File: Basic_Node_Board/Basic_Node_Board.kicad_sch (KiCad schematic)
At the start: 0 parts

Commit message: mh_initial_node_board_edits
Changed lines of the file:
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@@
 	(sheet
 		(at 31.75 88.9)
-		(size 72.39 45.72)
+		(size 90.17 76.2)
 		(fields_autoplaced yes)
 		(stroke
@@
 		)
 		(property "Sheetfile" "microcontroller.kicad_sch"
-			(at 31.75 135.2046 0)
+			(at 31.75 165.6846 0)
 			(effects
 				(font

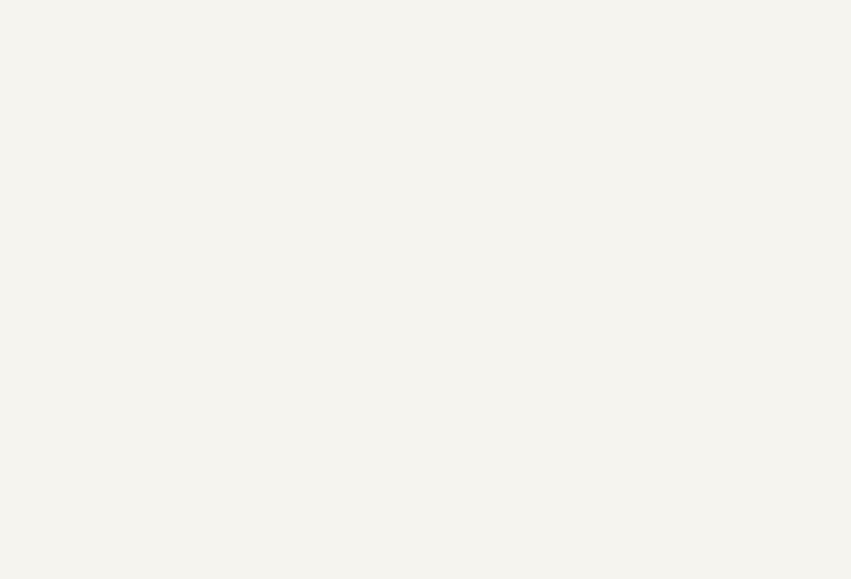
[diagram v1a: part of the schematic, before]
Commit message: Adding Buck Converter Schematic/Footprints
Added footprints to main pcb. Removing duplicate footprints (might cause problems, we will find out).
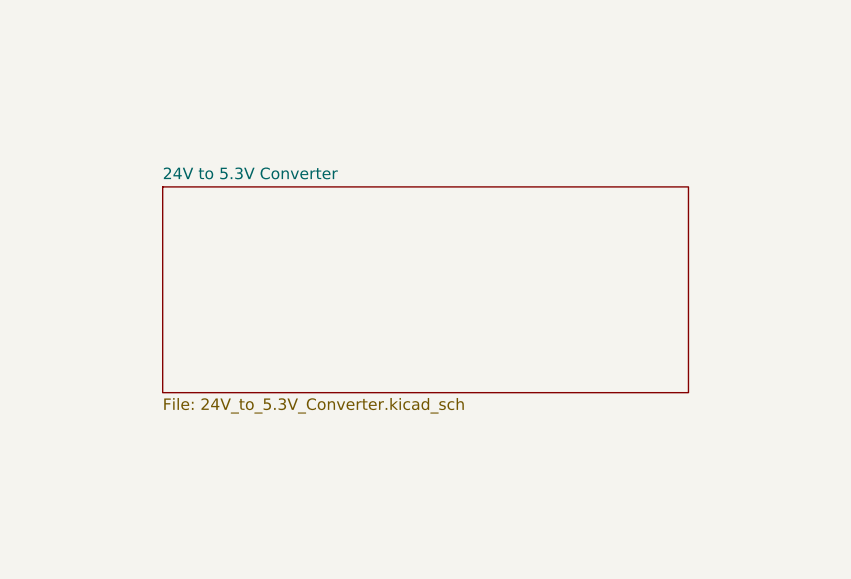
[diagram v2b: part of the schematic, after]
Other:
- added sheet 24V to 5.3V Converter (24V_to_5.3V_Converter.kicad_sch)
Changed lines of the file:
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@@
 (kicad_sch
-	(version 20231120)
+	(version 20250114)
 	(generator "eeschema")
-	(generator_version "8.0")
+	(generator_version "9.0")
 	(paper "A4")
 	(title_block
@@
 	)
 	(sheet
+		(at 156.21 95.25)
+		(size 58.42 22.86)
+		(exclude_from_sim no)
+		(in_bom yes)
+		(on_board yes)
+		(dnp no)
+		(fields_autoplaced yes)
+		(stroke
+			(width 0.1524)
+			(type solid)
+		)
+		(fill
+			(color 0 0 0 0.0000)
+		)
+		(property "Sheetname" "24V to 5.3V Converter"
+			(at 156.21 94.5384 0)
+			(effects
+				(font
+					(size 1.27 1.27)
+				)
+				(justify left bottom)
+			)
+		)
+		(property "Sheetfile" "24V_to_5.3V_Converter.kicad_sch"
+			(at 156.21 118.6946 0)
+			(effects
+				(font
+					(size 1.27 1.27)
+				)
+				(justify left top)
+			)
+		)
+		(instances
+			(project "Basic_Node_Board"
+				(path "/9602f2a9-59de-4c89-af09-0033871e87a5"
+					(page "5")
+				)
+			)
+		)
+	)
+	(sheet
 		(at 152.4 21.59)
 		(size 83.82 45.72)
+		(exclude_from_sim no)
+		(in_bom yes)
+		(on_board yes)
+		(dnp no)
 		(fields_autoplaced yes)
 		(stroke
@@
 		(at 31.75 88.9)
 		(size 90.17 76.2)
+		(exclude_from_sim no)
+		(in_bom yes)
+		(on_board yes)
+		(dnp no)
 		(fields_autoplaced yes)
 		(stroke
@@
 		(at 31.75 22.86)
 		(size 66.04 45.72)
+		(exclude_from_sim no)
+		(in_bom yes)
+		(on_board yes)
+		(dnp no)
 		(fields_autoplaced yes)
 		(stroke
@@
 		)
 	)
+	(embedded_fonts no)
 )

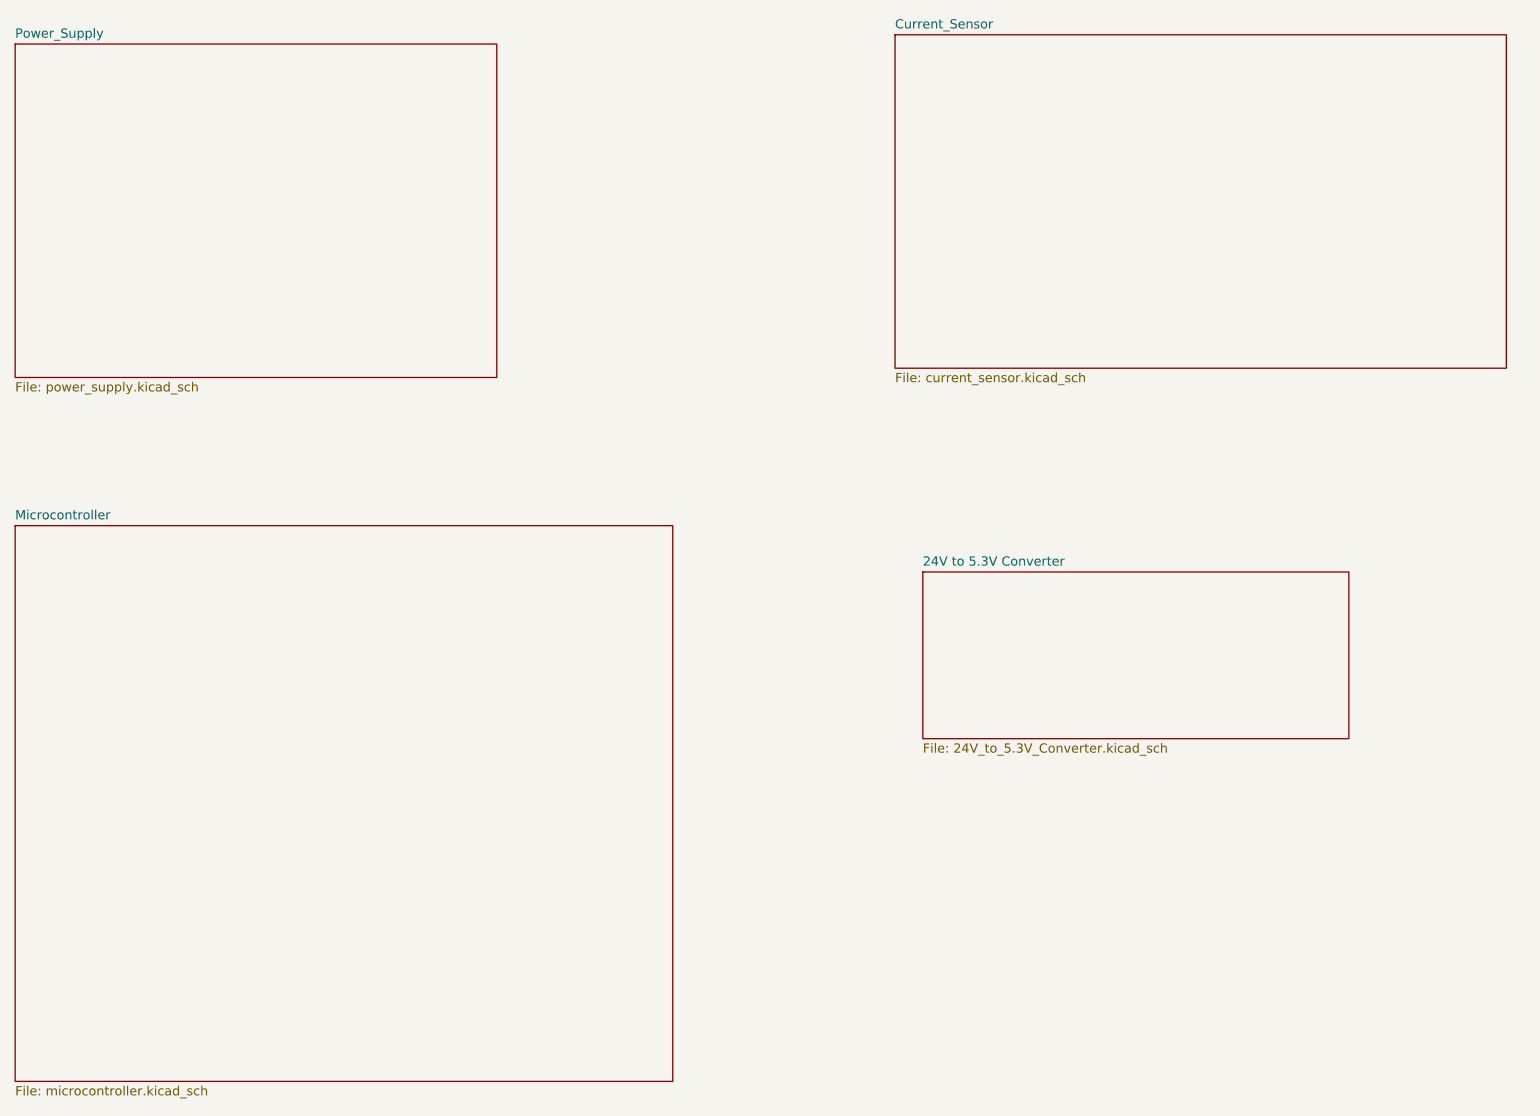
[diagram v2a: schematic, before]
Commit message: Power Distribution PCB KiCAD Schematic
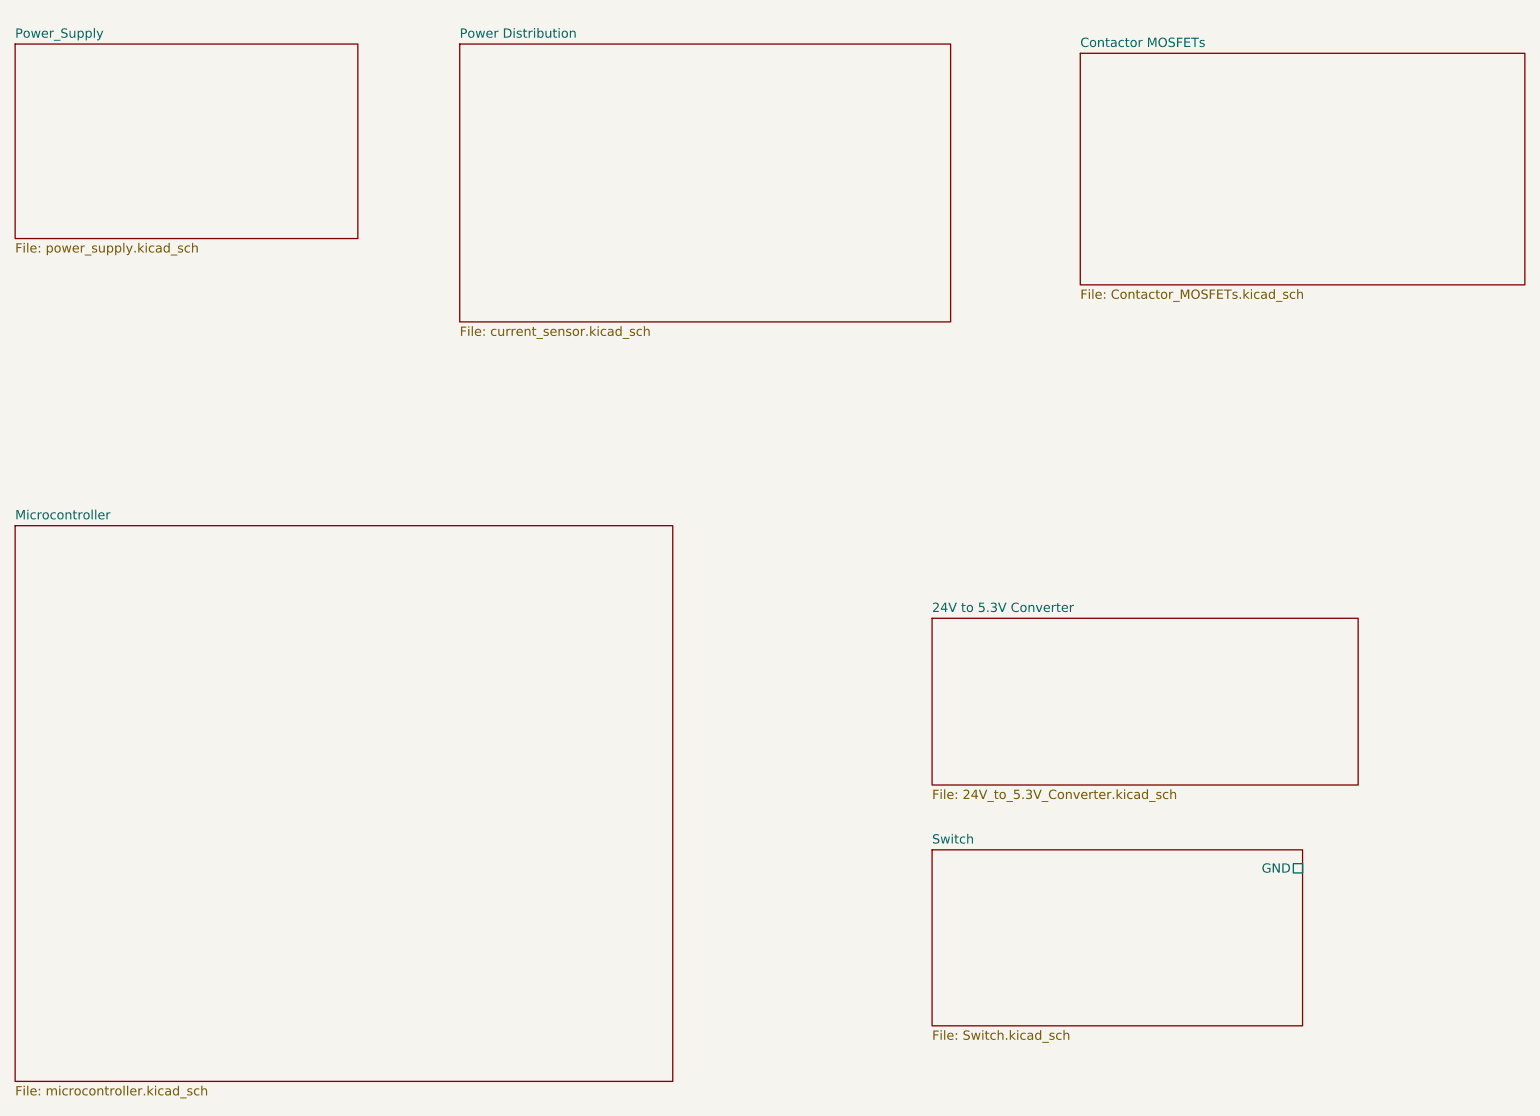
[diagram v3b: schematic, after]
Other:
- sheet Current_Sensor renamed Power Distribution
- added sheet Contactor MOSFETs (Contactor_MOSFETs.kicad_sch)
- added sheet Switch (Switch.kicad_sch)
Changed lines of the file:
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@@
 	)
 	(sheet
-		(at 156.21 95.25)
+		(at 157.48 101.6)
 		(size 58.42 22.86)
 		(exclude_from_sim no)
@@
 		)
 		(property "Sheetname" "24V to 5.3V Converter"
-			(at 156.21 94.5384 0)
+			(at 157.48 100.8884 0)
 			(effects
 				(font
@@
 		)
 		(property "Sheetfile" "24V_to_5.3V_Converter.kicad_sch"
-			(at 156.21 118.6946 0)
+			(at 157.48 125.0446 0)
 			(effects
 				(font
@@
 	)
 	(sheet
-		(at 152.4 21.59)
-		(size 83.82 45.72)
-		(exclude_from_sim no)
-		(in_bom yes)
-		(on_board yes)
-		(dnp no)
-		(fields_autoplaced yes)
-		(stroke
-			(width 0.1524)
-			(type solid)
-		)
-		(fill
-			(color 0 0 0 0.0000)
-		)
-		(property "Sheetname" "Current_Sensor"
-			(at 152.4 20.8784 0)
+		(at 92.71 22.86)
+		(size 67.31 38.1)
+		(exclude_from_sim no)
+		(in_bom yes)
+		(on_board yes)
+		(dnp no)
+		(fields_autoplaced yes)
+		(stroke
+			(width 0.1524)
+			(type solid)
+		)
+		(fill
+			(color 0 0 0 0.0000)
+		)
+		(property "Sheetname" "Power Distribution"
+			(at 92.71 22.1484 0)
 			(effects
 				(font
@@
 		)
 		(property "Sheetfile" "current_sensor.kicad_sch"
-			(at 152.4 67.8946 0)
+			(at 92.71 61.5446 0)
 			(effects
 				(font
@@
 	)
 	(sheet
+		(at 157.48 133.35)
+		(size 50.8 24.13)
+		(exclude_from_sim no)
+		(in_bom yes)
+		(on_board yes)
+		(dnp no)
+		(fields_autoplaced yes)
+		(stroke
+			(width 0.1524)
+			(type solid)
+		)
+		(fill
+			(color 0 0 0 0.0000)
+		)
+		(property "Sheetname" "Switch"
+			(at 157.48 132.6384 0)
+			(effects
+				(font
+					(size 1.27 1.27)
+				)
+				(justify left bottom)
+			)
+		)
+		(property "Sheetfile" "Switch.kicad_sch"
+			(at 157.48 158.0646 0)
+			(effects
+				(font
+					(size 1.27 1.27)
+				)
+				(justify left top)
+			)
+		)
+		(pin "GND" passive
+			(at 208.28 135.89 0)
+			(effects
+				(font
+					(size 1.27 1.27)
+				)
+				(justify right)
+			)
+		)
+		(instances
+			(project "Basic_Node_Board"
+				(path "/9602f2a9-59de-4c89-af09-0033871e87a5"
+					(page "6")
+				)
+			)
+		)
+	)
+	(sheet
+		(at 177.8 24.13)
+		(size 60.96 31.75)
+		(exclude_from_sim no)
+		(in_bom yes)
+		(on_board yes)
+		(dnp no)
+		(fields_autoplaced yes)
+		(stroke
+			(width 0.1524)
+			(type solid)
+		)
+		(fill
+			(color 0 0 0 0.0000)
+		)
+		(property "Sheetname" "Contactor MOSFETs"
+			(at 177.8 23.4184 0)
+			(effects
+				(font
+					(size 1.27 1.27)
+				)
+				(justify left bottom)
+			)
+		)
+		(property "Sheetfile" "Contactor_MOSFETs.kicad_sch"
+			(at 177.8 56.4646 0)
+			(effects
+				(font
+					(size 1.27 1.27)
+				)
+				(justify left top)
+			)
+		)
+		(instances
+			(project "Basic_Node_Board"
+				(path "/9602f2a9-59de-4c89-af09-0033871e87a5"
+					(page "8")
+				)
+			)
+		)
+	)
+	(sheet
 		(at 31.75 22.86)
-		(size 66.04 45.72)
+		(size 46.99 26.67)
 		(exclude_from_sim no)
 		(in_bom yes)
@@
 		)
 		(property "Sheetfile" "power_supply.kicad_sch"
-			(at 31.75 69.1646 0)
-			(effects
-				(font
+			(at 31.75 50.1146 0)
+			(effects
+				(font
